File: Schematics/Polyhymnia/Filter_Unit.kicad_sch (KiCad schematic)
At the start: 3 parts, among them J2 Conn_02x02_Counter_Clockwise

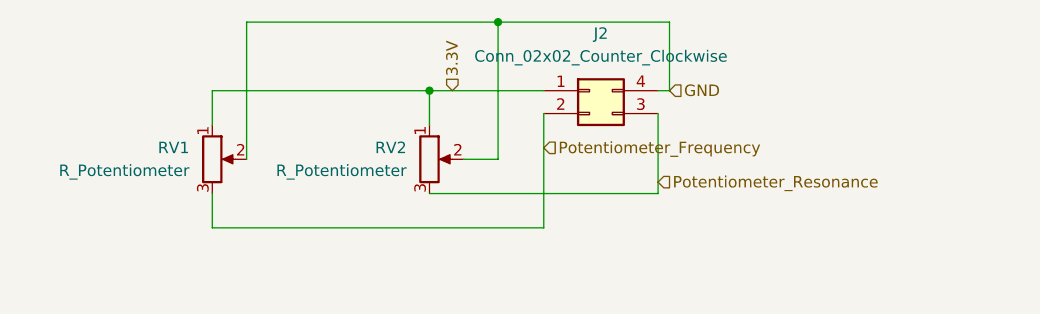
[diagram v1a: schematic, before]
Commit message: Added audio amplifier schematics
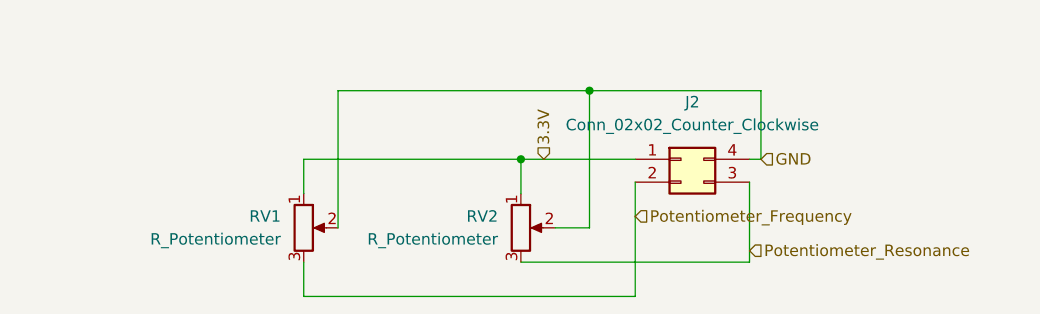
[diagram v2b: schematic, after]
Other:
- title: (none) -> Filter Control Unit
- moved on the sheet: J2, RV1, RV2
